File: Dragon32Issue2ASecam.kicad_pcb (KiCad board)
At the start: 2 copper layers, 253 x 199.1 mm, 20 parts, among them IC17 68A364, IC18 68A364, IC19 MC6809E, SW1 RESET

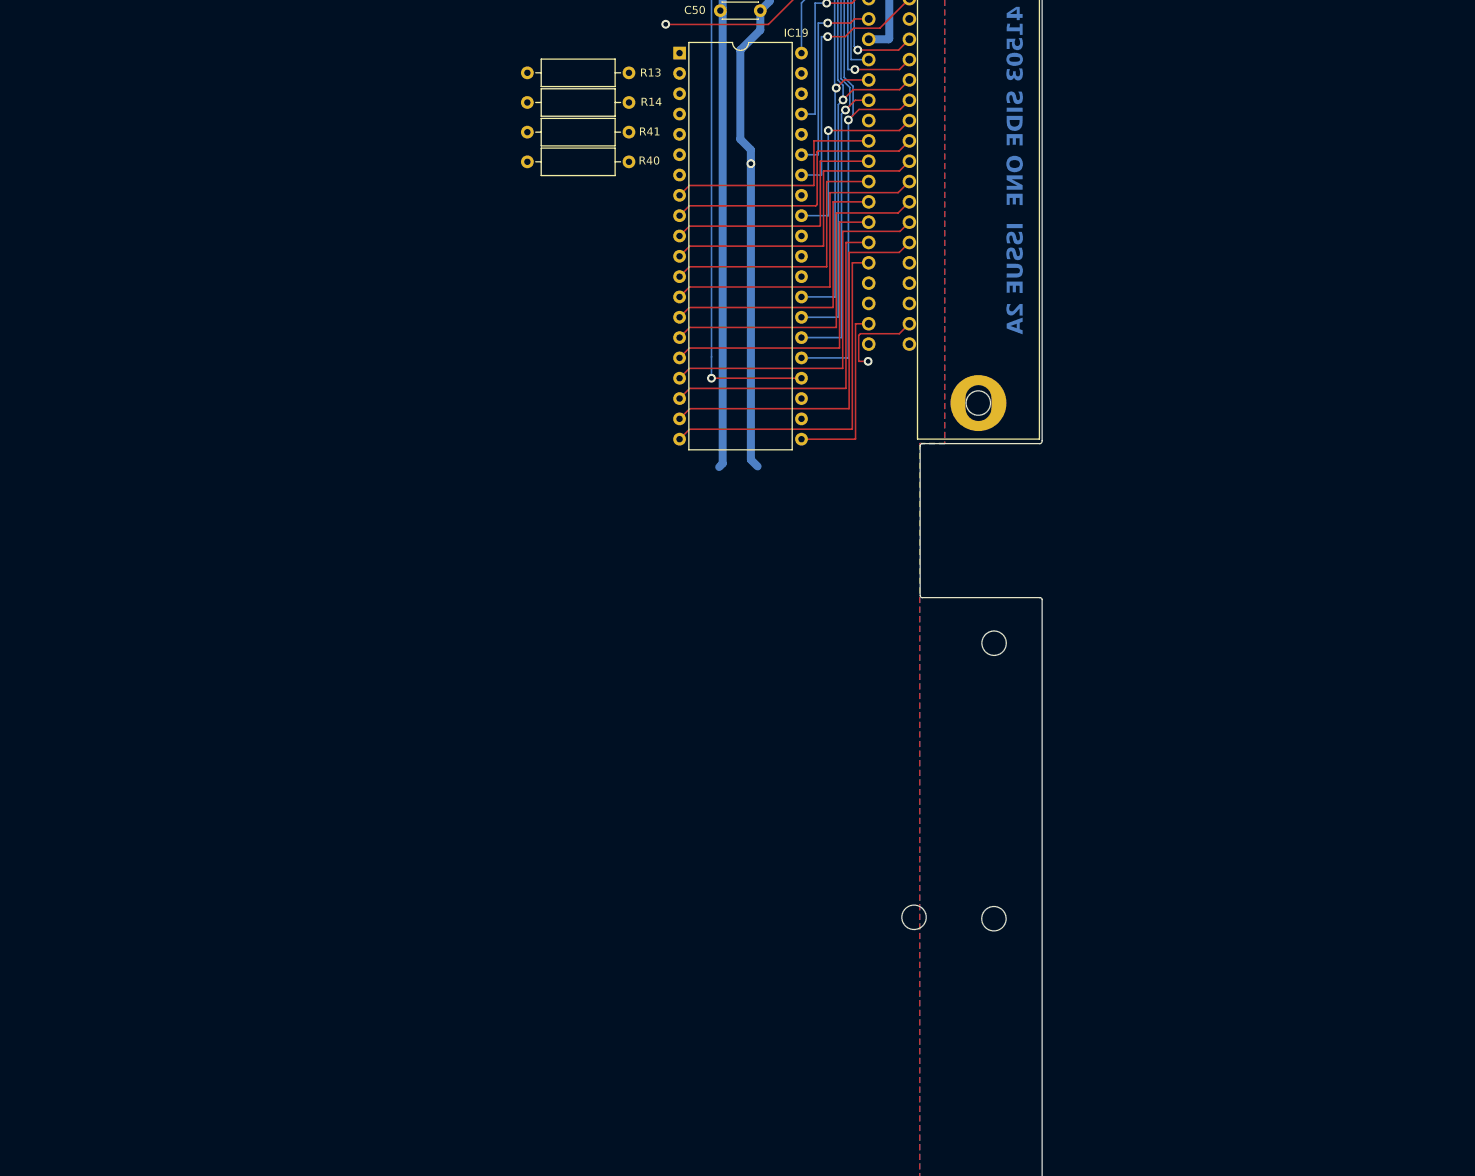
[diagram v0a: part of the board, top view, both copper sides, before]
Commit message: add sam and ram
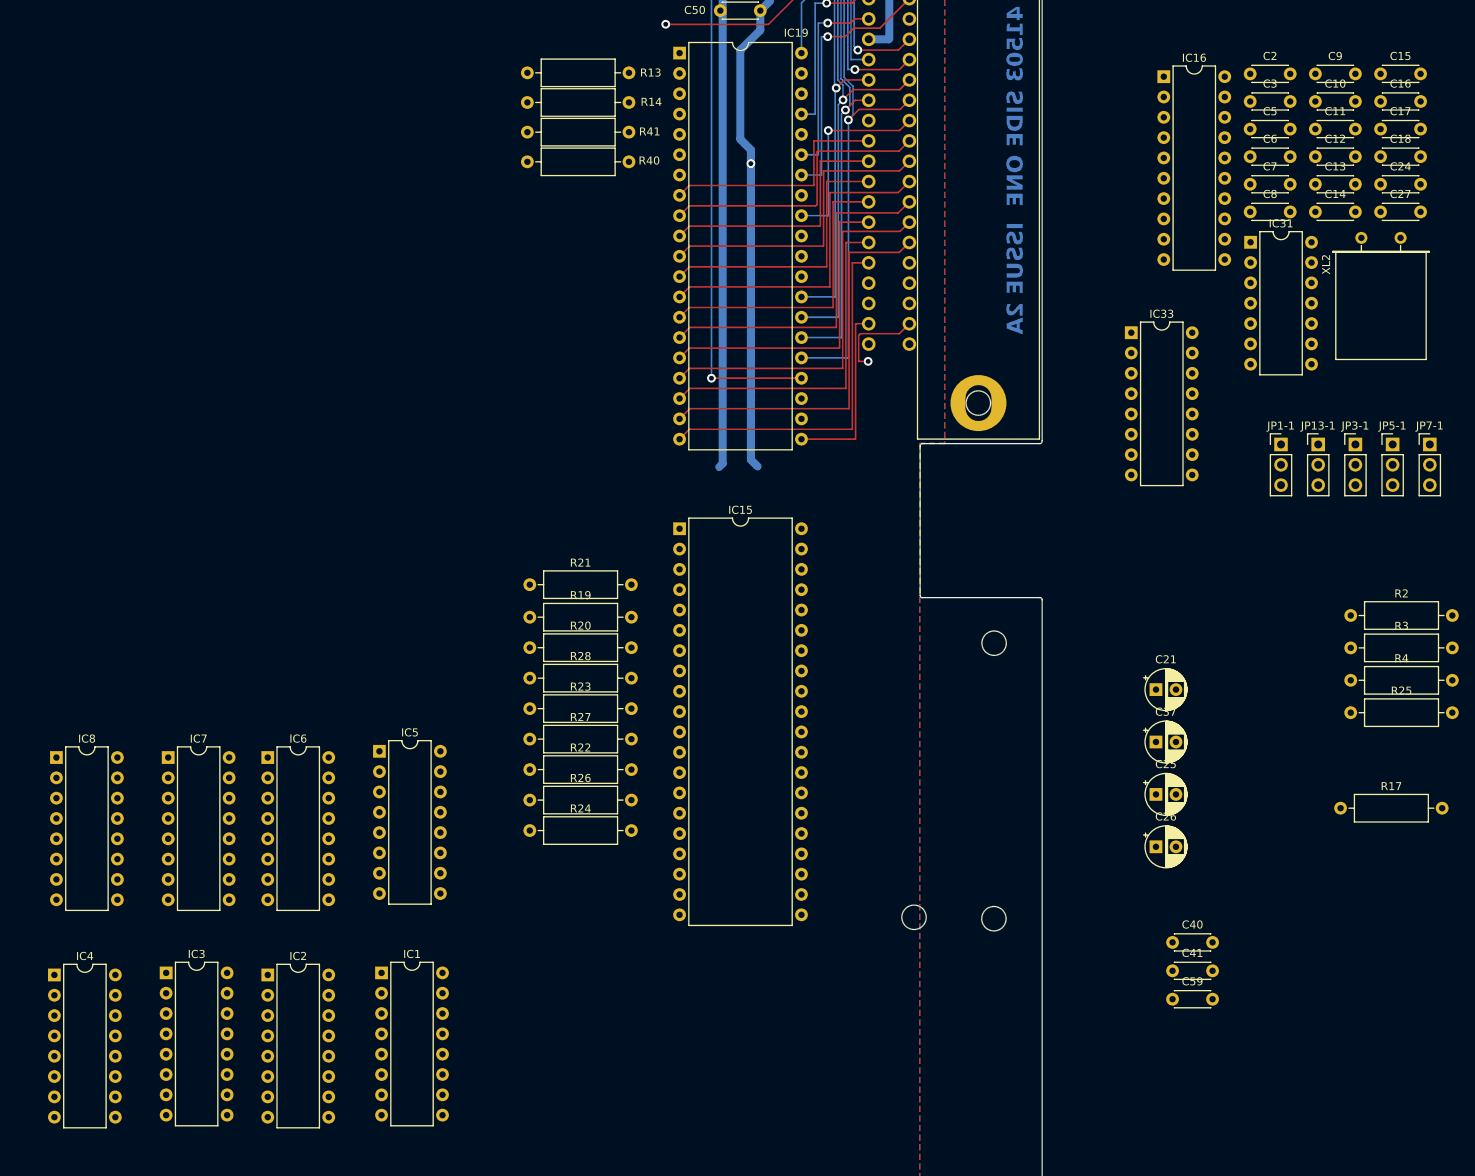
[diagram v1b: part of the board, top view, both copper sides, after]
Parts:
- added C10: 0.1uF, Capacitor_THT:C_Disc_D4.3mm_W1.9mm_P5.00mm, F.Cu at (373.8, 106.7)
- added C11: 0.1uF, Capacitor_THT:C_Disc_D4.3mm_W1.9mm_P5.00mm, F.Cu at (373.8, 110.2)
- added C12: 0.1uF, Capacitor_THT:C_Disc_D4.3mm_W1.9mm_P5.00mm, F.Cu at (373.8, 113.6)
- added C13: 0.1uF, Capacitor_THT:C_Disc_D4.3mm_W1.9mm_P5.00mm, F.Cu at (373.8, 117.1)
- added C14: 0.1uF, Capacitor_THT:C_Disc_D4.3mm_W1.9mm_P5.00mm, F.Cu at (373.8, 120.5)
- added C15: 0.1uF, Capacitor_THT:C_Disc_D4.3mm_W1.9mm_P5.00mm, F.Cu at (381.9, 103.3)
- added C16: 0.1uF, Capacitor_THT:C_Disc_D4.3mm_W1.9mm_P5.00mm, F.Cu at (381.9, 106.7)
- added C17: 0.1uF, Capacitor_THT:C_Disc_D4.3mm_W1.9mm_P5.00mm, F.Cu at (381.9, 110.2)
- added C18: 0.1uF, Capacitor_THT:C_Disc_D4.3mm_W1.9mm_P5.00mm, F.Cu at (381.9, 113.6)
- added C2: 0.1uF, Capacitor_THT:C_Disc_D4.3mm_W1.9mm_P5.00mm, F.Cu at (365.6, 103.3)
- added C21: 4.7uF, Capacitor_THT:CP_Radial_D5.0mm_P2.50mm, F.Cu at (353.9, 180.2)
- added C24: 0.1uF, Capacitor_THT:C_Disc_D4.3mm_W1.9mm_P5.00mm, F.Cu at (381.9, 117.1)
- added C25: 10uF, Capacitor_THT:CP_Radial_D5.0mm_P2.50mm, F.Cu at (353.9, 193.3)
- added C26: 4.7uF, Capacitor_THT:CP_Radial_D5.0mm_P2.50mm, F.Cu at (353.9, 199.9)
- added C27: 0.01uF, Capacitor_THT:C_Disc_D4.3mm_W1.9mm_P5.00mm, F.Cu at (381.9, 120.5)
- added C3: 0.1uF, Capacitor_THT:C_Disc_D4.3mm_W1.9mm_P5.00mm, F.Cu at (365.6, 106.7)
- added C37: 4.7uF, Capacitor_THT:CP_Radial_D5.0mm_P2.50mm, F.Cu at (353.9, 186.8)
- added C40: 22pF, Capacitor_THT:C_Disc_D4.3mm_W1.9mm_P5.00mm, F.Cu at (355.9, 211.8)
- added C41: 33pF, Capacitor_THT:C_Disc_D4.3mm_W1.9mm_P5.00mm, F.Cu at (355.9, 215.4)
- added C5: 0.1uF, Capacitor_THT:C_Disc_D4.3mm_W1.9mm_P5.00mm, F.Cu at (365.6, 110.2)
- added C59: 33pF, Capacitor_THT:C_Disc_D4.3mm_W1.9mm_P5.00mm, F.Cu at (355.9, 218.9)
- added C6: 0.1uF, Capacitor_THT:C_Disc_D4.3mm_W1.9mm_P5.00mm, F.Cu at (365.6, 113.6)
- added C7: 0.1uF, Capacitor_THT:C_Disc_D4.3mm_W1.9mm_P5.00mm, F.Cu at (365.6, 117.1)
- added C8: 0.1uF, Capacitor_THT:C_Disc_D4.3mm_W1.9mm_P5.00mm, F.Cu at (365.6, 120.5)
- added C9: 0.1uF, Capacitor_THT:C_Disc_D4.3mm_W1.9mm_P5.00mm, F.Cu at (373.8, 103.3)
- added IC1: HYB4116, Package_DIP:DIP-16_W7.62mm, F.Cu at (257.1, 215.7)
- added IC15: MC6883, Package_DIP:DIP-40_W15.24mm, F.Cu at (294.3, 160.1)
- added IC16: 74LS244N, Package_DIP:DIP-20_W7.62mm, F.Cu at (354.8, 103.6)
- added IC2: HYB4116, Package_DIP:DIP-16_W7.62mm, F.Cu at (242.8, 215.9)
- added IC3: HYB4116, Package_DIP:DIP-16_W7.62mm, F.Cu at (230.1, 215.7)
- added IC31: 74LS02N, Package_DIP:DIP-14_W7.62mm, F.Cu at (365.7, 124.3)
- added IC33: 74LS138N, Package_DIP:DIP-16_W7.62mm, F.Cu at (350.8, 135.6)
- added IC4: HYB4116, Package_DIP:DIP-16_W7.62mm, F.Cu at (216.2, 215.9)
- added IC5: HYB4116, Package_DIP:DIP-16_W7.62mm, F.Cu at (256.8, 188.0)
- added IC6: HYB4116, Package_DIP:DIP-16_W7.62mm, F.Cu at (242.8, 188.7)
- added IC7: HYB4116, Package_DIP:DIP-16_W7.62mm, F.Cu at (230.4, 188.7)
- added IC8: HYB4116, Package_DIP:DIP-16_W7.62mm, F.Cu at (216.4, 188.7)
- added JP1-1: 1 low, Connector_PinHeader_2.54mm:PinHeader_1x03_P2.54mm_Vertical, F.Cu at (369.5, 149.6)
- added JP13-1: 32k/64k, Connector_PinHeader_2.54mm:PinHeader_1x03_P2.54mm_Vertical, F.Cu at (374.1, 149.6)
- added JP3-1: 16k/32k, Connector_PinHeader_2.54mm:PinHeader_1x03_P2.54mm_Vertical, F.Cu at (378.8, 149.6)
- added JP5-1: 16k/32k, Connector_PinHeader_2.54mm:PinHeader_1x03_P2.54mm_Vertical, F.Cu at (383.4, 149.6)
- added JP7-1: 16k/32k, Connector_PinHeader_2.54mm:PinHeader_1x03_P2.54mm_Vertical, F.Cu at (388.1, 149.6)
- added R17: 1K5, Resistor_THT:R_Axial_DIN0309_L9.0mm_D3.2mm_P12.70mm_Horizontal, F.Cu at (376.9, 195.1)
- added R19: 22R, Resistor_THT:R_Axial_DIN0309_L9.0mm_D3.2mm_P12.70mm_Horizontal, F.Cu at (275.6, 171.2)
- added R2: 4K7, Resistor_THT:R_Axial_DIN0309_L9.0mm_D3.2mm_P12.70mm_Horizontal, F.Cu at (378.2, 171.0)
- added R20: 22R, Resistor_THT:R_Axial_DIN0309_L9.0mm_D3.2mm_P12.70mm_Horizontal, F.Cu at (275.6, 175.0)
- added R21: 22R, Resistor_THT:R_Axial_DIN0309_L9.0mm_D3.2mm_P12.70mm_Horizontal, F.Cu at (275.6, 167.1)
- added R22: 22R, Resistor_THT:R_Axial_DIN0309_L9.0mm_D3.2mm_P12.70mm_Horizontal, F.Cu at (275.6, 190.2)
- added R23: 22R, Resistor_THT:R_Axial_DIN0309_L9.0mm_D3.2mm_P12.70mm_Horizontal, F.Cu at (275.6, 182.6)
- added R24: 22R, Resistor_THT:R_Axial_DIN0309_L9.0mm_D3.2mm_P12.70mm_Horizontal, F.Cu at (275.6, 197.9)
- added R25: 22R, Resistor_THT:R_Axial_DIN0309_L9.0mm_D3.2mm_P12.70mm_Horizontal, F.Cu at (378.2, 183.1)
- added R26: 22R, Resistor_THT:R_Axial_DIN0309_L9.0mm_D3.2mm_P12.70mm_Horizontal, F.Cu at (275.6, 194.1)
- added R27: 22R, Resistor_THT:R_Axial_DIN0309_L9.0mm_D3.2mm_P12.70mm_Horizontal, F.Cu at (275.6, 186.4)
- added R28: 22R, Resistor_THT:R_Axial_DIN0309_L9.0mm_D3.2mm_P12.70mm_Horizontal, F.Cu at (275.6, 178.8)
- added R3: 1K5, Resistor_THT:R_Axial_DIN0309_L9.0mm_D3.2mm_P12.70mm_Horizontal, F.Cu at (378.2, 175.0)
- added R4: 22R, Resistor_THT:R_Axial_DIN0309_L9.0mm_D3.2mm_P12.70mm_Horizontal, F.Cu at (378.2, 179.1)
- added XL2: 14.31818MHz, Crystal:Crystal_HC49-U_Horizontal, F.Cu at (379.5, 123.8)

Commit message: work on memory sub system
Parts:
- removed C10, C11, C12, C13, C2, C24, C3, C5, C6, C7, C8, C9: 0.1uF, Capacitor_THT:C_Disc_D4.3mm_W1.9mm_P5.00mm
- removed C25: 10uF, Capacitor_THT:CP_Radial_D5.0mm_P2.50mm
- removed C26: 4.7uF, Capacitor_THT:CP_Radial_D5.0mm_P2.50mm
- removed C27: 0.01uF, Capacitor_THT:C_Disc_D4.3mm_W1.9mm_P5.00mm
- removed C59: 33pF, Capacitor_THT:C_Disc_D4.3mm_W1.9mm_P5.00mm
- removed JP1-1: 1 low, Connector_PinHeader_2.54mm:PinHeader_1x03_P2.54mm_Vertical
- removed JP13-1: 32k/64k, Connector_PinHeader_2.54mm:PinHeader_1x03_P2.54mm_Vertical
- removed JP3-1, JP5-1, JP7-1: 16k/32k, Connector_PinHeader_2.54mm:PinHeader_1x03_P2.54mm_Vertical
- removed R17, R3: 1K5, Resistor_THT:R_Axial_DIN0309_L9.0mm_D3.2mm_P12.70mm_Horizontal
- removed R2: 4K7, Resistor_THT:R_Axial_DIN0309_L9.0mm_D3.2mm_P12.70mm_Horizontal
- removed R4: 22R, Resistor_THT:R_Axial_DIN0309_L9.0mm_D3.2mm_P12.70mm_Horizontal
- added C19: 0.1uF, Capacitor_THT:C_Disc_D4.3mm_W1.9mm_P5.00mm, F.Cu at (223.7, 214.8)
- added C20: 0.1uF, Capacitor_THT:C_Disc_D4.3mm_W1.9mm_P5.00mm, F.Cu at (240.1, 214.8)
- added C51: 0.1uF, Capacitor_THT:C_Disc_D4.3mm_W1.9mm_P5.00mm, F.Cu at (298.2, 157.6)
- added LK2: LK2, Connector_PinHeader_2.54mm:PinHeader_1x03_P2.54mm_Vertical, F.Cu at (270.1, 226.4)
- added R12: 22R, Dragon:R_Axial_DIN0309_L9.0mm_D2.5mm_P12.70mm_Horizontal, F.Cu at (271.0, 207.7)
- added R37: 1K5, Dragon:R_Axial_DIN0309_L9.0mm_D2.5mm_P12.70mm_Horizontal, F.Cu at (308.5, 182.3)
- added R39: 4K7, Dragon:R_Axial_DIN0309_L9.0mm_D2.5mm_P12.70mm_Horizontal, F.Cu at (271.0, 210.3)
- C21: value 4.7uF -> 0.1uF; footprint Capacitor_THT:CP_Radial_D5.0mm_P2.50mm -> Capacitor_THT:C_Disc_D4.3mm_W1.9mm_P5.00mm
- C37: footprint Capacitor_THT:CP_Radial_D5.0mm_P2.50mm -> Capacitor_THT:CP_Radial_Tantal_D5.5mm_P5.00mm
- C40: footprint Capacitor_THT:C_Disc_D4.3mm_W1.9mm_P5.00mm -> Dragon:C_Radial_Special
- C41: footprint Capacitor_THT:C_Disc_D4.3mm_W1.9mm_P5.00mm -> Capacitor_THT:C_Disc_D3.0mm_W1.6mm_P2.50mm
- IC1, IC2, IC3, IC4, IC5, IC6, IC7, IC8: value HYB4116 -> M3732H-20RS
- R1, R13, R14, R19, R20, R21, R22, R23, R24, R25, R26, R27, R28, R36, R40, R41: footprint Resistor_THT:R_Axial_DIN0309_L9.0mm_D3.2mm_P12.70mm_Horizontal -> Dragon:R_Axial_DIN0309_L9.0mm_D2.5mm_P12.70mm_Horizontal
- moved C18 201.3 mm to (207.9, 214.8)
- moved C15 179.5 mm to (223.8, 188.2)
- moved C14 179.3 mm to (207.7, 188.2)
- moved C16 163.6 mm to (240.0, 188.2)
- moved C17 148.3 mm to (255.8, 188.2)
- moved IC31 132.7 mm to (275.2, 221.4)
- moved IC16 115.1 mm to (254.6, 160.2)
- moved R25 109.5 mm to (271.0, 205.2)
- moved C21 103.7 mm to (256.1, 214.8)
- moved IC33 98.6 mm to (298.0, 218.9)
- moved XL2 91.8 mm to (311.2, 185.0)
- moved C41 60.7 mm to (308.6, 177.4)
- moved C40 60.1 mm to (313.8, 169.0)
- moved IC5 59.0 mm to (206.5, 218.9)
- moved IC1 55.6 mm to (206.5, 192.5)
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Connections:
- C14 pad 1: RAM VBB -> RAM VCC
- C15 pad 1: GND -> RAM VCC
- C15 pad 2: RAM VDD -> GND
- C16 pad 1: GND -> RAM VCC
- C16 pad 2: RAM VDD -> GND
- C17 pad 1: RAM VBB -> RAM VCC
- C18 pad 1: RAM VBB -> RAM VCC
- C21 pad 1: GND -> RAM VCC
- C21 pad 2: -5V -> GND
- C41 pad 1: GND -> Net-(C41-Pad1)
- C41 pad 2: Net-(C41-Pad2) -> GND
- IC1 pad 1: RAM VBB -> unconnected-(IC1-NC-Pad1)
- IC1 pad 8: RAM VDD -> RAM VCC
- IC1 pad 9: RAM VCC -> nZ7
- IC2 pad 1: RAM VBB -> unconnected-(IC2-NC-Pad1)
- IC2 pad 8: RAM VDD -> RAM VCC
- IC2 pad 9: RAM VCC -> nZ7
- IC3 pad 1: RAM VBB -> unconnected-(IC3-NC-Pad1)
- IC3 pad 8: RAM VDD -> RAM VCC
- IC3 pad 9: RAM VCC -> nZ7
- IC31 pad 1: Net-(IC33-E2) -> Net-(LK2-B)
- IC31 pad 10: (no net) -> Net-(IC33-E2)
- IC31 pad 2: R/~{W} -> Z7
- IC31 pad 3: S2 -> Z7
- IC31 pad 4: Net-(JP1-1-B) -> (no net)
- IC31 pad 5: Z7 -> (no net)
- IC31 pad 6: Z7 -> (no net)
- IC31 pad 8: (no net) -> R/~{W}
- IC31 pad 9: (no net) -> S2
- IC4 pad 1: RAM VBB -> unconnected-(IC4-NC-Pad1)
- IC4 pad 8: RAM VDD -> RAM VCC
- IC4 pad 9: RAM VCC -> nZ7
- IC5 pad 1: RAM VBB -> unconnected-(IC5-NC-Pad1)
- IC5 pad 8: RAM VDD -> RAM VCC
- IC5 pad 9: RAM VCC -> nZ7
- IC6 pad 1: RAM VBB -> unconnected-(IC6-NC-Pad1)
- IC6 pad 8: RAM VDD -> RAM VCC
- IC6 pad 9: RAM VCC -> nZ7
- IC7 pad 1: RAM VBB -> unconnected-(IC7-NC-Pad1)
- IC7 pad 8: RAM VDD -> RAM VCC
- IC7 pad 9: RAM VCC -> nZ7
- IC8 pad 1: RAM VBB -> unconnected-(IC8-NC-Pad1)
- IC8 pad 8: RAM VDD -> RAM VCC
- IC8 pad 9: RAM VCC -> nZ7
- R23 pad 1: Z2 -> Z1
- R24 pad 1: Z1 -> Z2
- R26 pad 1: ~{RAS0} -> ~{CAS}
- R26 pad 2: Net-(IC15-~{RAS0}) -> Net-(IC15-~{CAS})
- R27 pad 1: ~{CAS} -> ~{RAS0}
- R27 pad 2: Net-(IC15-~{CAS}) -> Net-(IC15-~{RAS0})
- XL2 pad 1: Net-(IC15-OSCIN) -> Net-(C41-Pad1)
- XL2 pad 2: Net-(C41-Pad2) -> Net-(IC15-OSCIN)
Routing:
- net Z5: track 0.00 -> 164.1 mm, vias 0 -> 2
- net Z4: track 0.00 -> 160.6 mm, vias 0 -> 3
- net Z6: track 0.00 -> 159.3 mm, vias 0 -> 1
- net Z3: track 0.00 -> 154.1 mm, vias 0 -> 2
- net RAM VCC: track 0.00 -> 149.5 mm
- net nZ7: track 0.00 -> 149.2 mm
- net ~{CAS}: track 0.00 -> 143.2 mm, vias 0 -> 2
- net GND: track 96.3 -> 238.2 mm, vias 0 -> 6
- net P2: track 0.00 -> 140.9 mm, vias 0 -> 1
- net ~{WE}: track 0.00 -> 124.8 mm, vias 0 -> 2
- net R2: track 0.00 -> 121.5 mm
- net ~{RAS0}: track 0.00 -> 119.7 mm, vias 0 -> 1
- net Z2: track 0.00 -> 119.7 mm, vias 0 -> 1
- net Z0: track 0.00 -> 117.6 mm, vias 0 -> 2
- net +5V: track 200.7 -> 302.5 mm, vias 1 -> 2
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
